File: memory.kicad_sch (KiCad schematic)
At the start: 22 parts, among them U2 IS42S16160J-6BLI, U3 MX30LF1G18AC-XKI, U4 KLM8G1GETF-B041

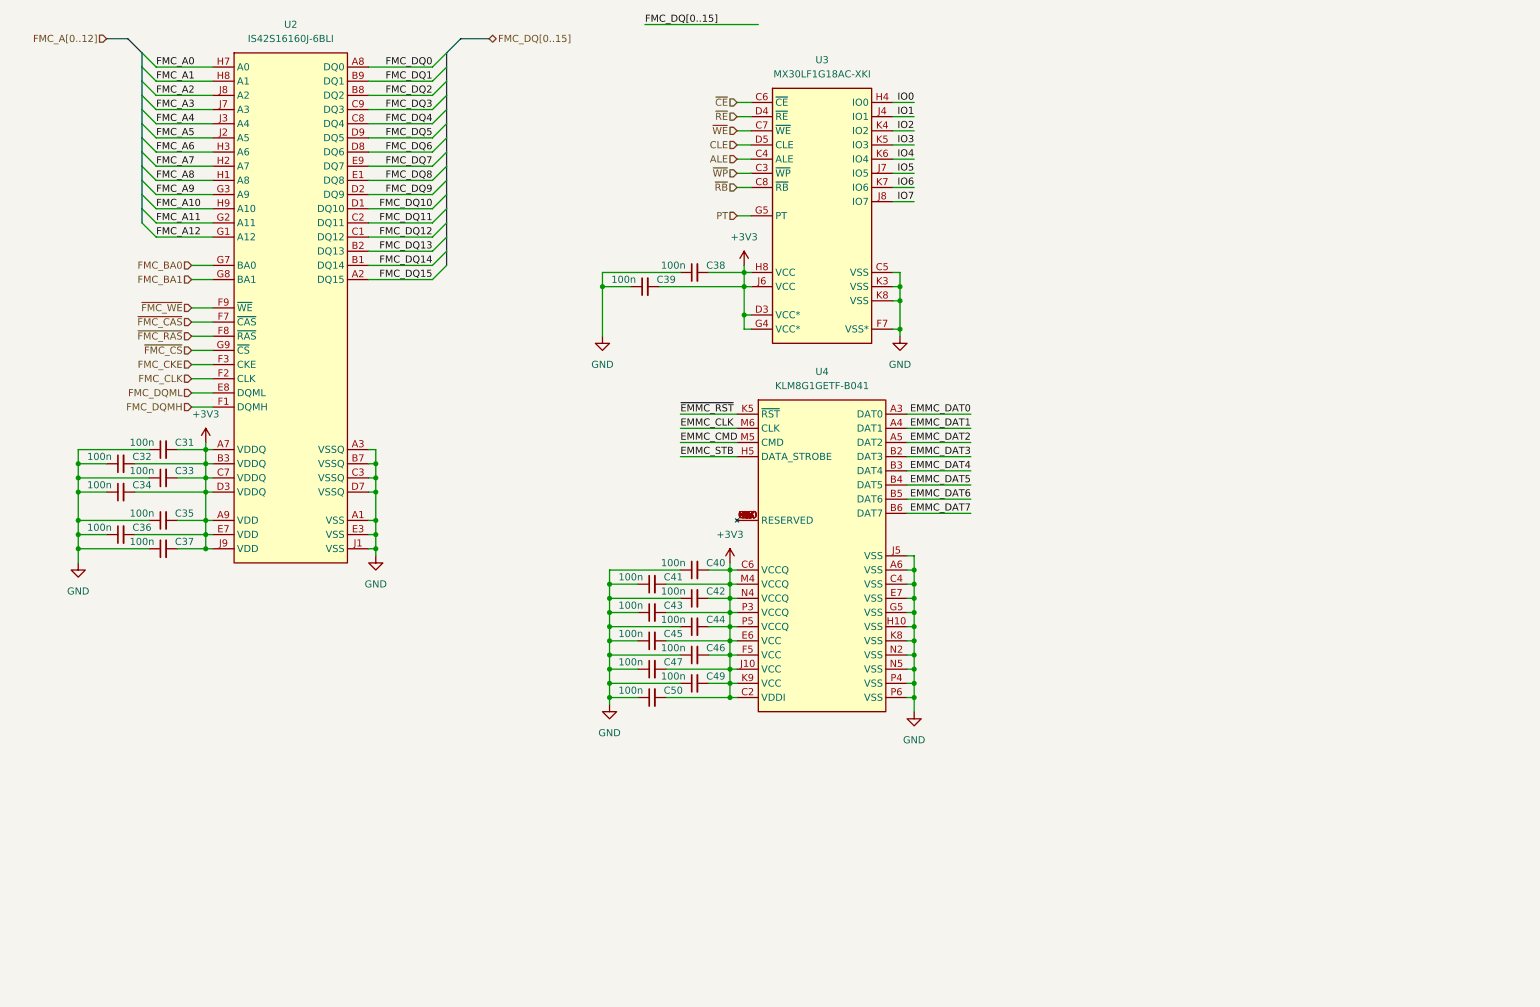
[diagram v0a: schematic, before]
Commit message: Added octospi flash lib
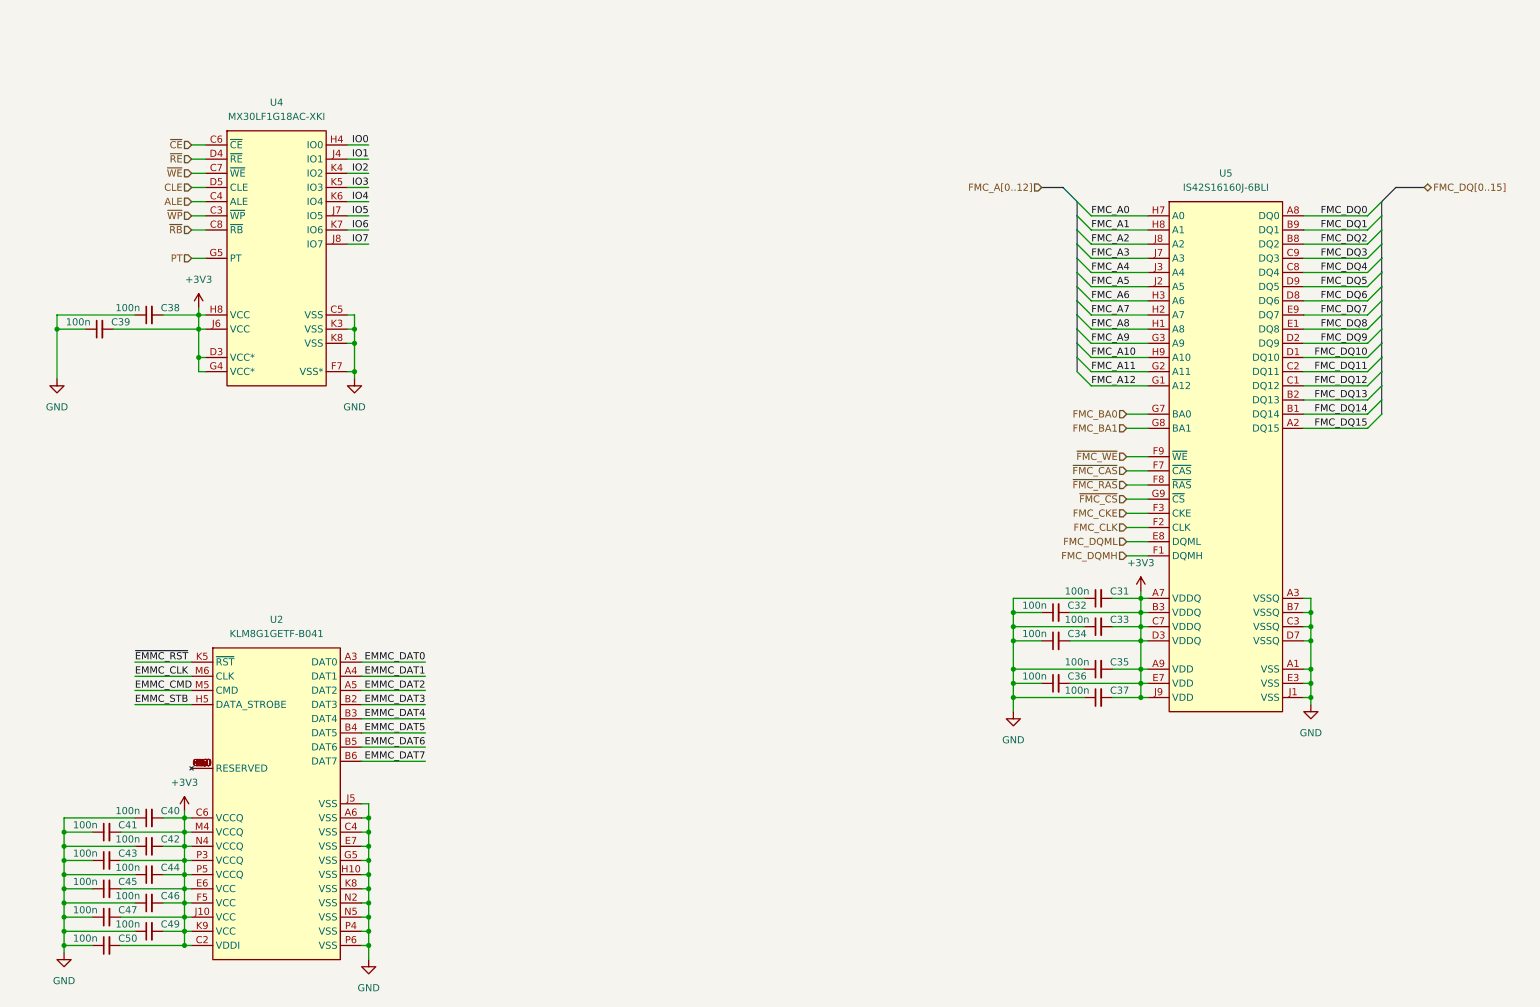
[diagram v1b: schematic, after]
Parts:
- removed U2: IS42S16160J-6BLI, IS42S16160J-6BLI (1):BGA54C80P9X9_800X800X120, symbol Memory_SDRAM:IS42S16160J-BLI-BGA
- removed U3: MX30LF1G18AC-XKI, lib:BGA63C80P10X12_900X1100X100N, symbol Memory_NAND_FLASH:MX30LF1G18AC-XKI
- removed U4: KLM8G1GETF-B041, KLM8G1GETF-B0410:BGA153C50P14X14_1150X1300X80, symbol Memory_EMMC:KLM8G1GETF-B041-Samsung
- added U2: KLM8G1GETF-B041, symbol Memory_EMMC:KLM8G1GETF-B041-Samsung
- added U4: MX30LF1G18AC-XKI, symbol Memory_NAND_FLASH:MX30LF1G18AC-XKI
- added U5: IS42S16160J-6BLI, symbol Memory_SDRAM:IS42S16160J-6BLI-BGA
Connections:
- net +3V3: now also U2.C2 (VDDI), U2.C6 (VCCQ), U2.E6 (VCC), U2.F5 (VCC), U2.J10 (VCC), U2.K9 (VCC), U2.M4 (VCCQ), U2.N4 (VCCQ), U2.P3 (VCCQ), U2.P5 (VCCQ), U4.D3 (VCC*), U4.G4 (VCC*), U4.H8 (VCC), U4.J6 (VCC), U5.A7 (VDDQ), U5.A9 (VDD), U5.B3 (VDDQ), U5.C7 (VDDQ), U5.D3 (VDDQ), U5.E7 (VDD), U5.J9 (VDD)
- net ALE: now also U4.C4 (ALE)
- net CLE: now also U4.D5 (CLE)
- net EMMC_CLK: now also U2.M6 (CLK)
- net EMMC_CMD: now also U2.M5 (CMD)
- net EMMC_DAT0: now also U2.A3 (DAT0)
- net EMMC_DAT1: now also U2.A4 (DAT1)
- net EMMC_DAT2: now also U2.A5 (DAT2)
- net EMMC_DAT3: now also U2.B2 (DAT3)
- net EMMC_DAT4: now also U2.B3 (DAT4)
- net EMMC_DAT5: now also U2.B4 (DAT5)
- net EMMC_DAT6: now also U2.B5 (DAT6)
- net EMMC_DAT7: now also U2.B6 (DAT7)
- net EMMC_STB: now also U2.H5 (DATA_STROBE)
- net FMC_A0: now also U5.H7 (A0)
- net FMC_A1: now also U5.H8 (A1)
- net FMC_A10: now also U5.H9 (A10)
- net FMC_A11: now also U5.G2 (A11)
- net FMC_A12: now also U5.G1 (A12)
- net FMC_A2: now also U5.J8 (A2)
- net FMC_A3: now also U5.J7 (A3)
- net FMC_A4: now also U5.J3 (A4)
- net FMC_A5: now also U5.J2 (A5)
- net FMC_A6: now also U5.H3 (A6)
- net FMC_A7: now also U5.H2 (A7)
- net FMC_A8: now also U5.H1 (A8)
- net FMC_A9: now also U5.G3 (A9)
- net FMC_BA0: now also U5.G7 (BA0)
- net FMC_BA1: now also U5.G8 (BA1)
- net FMC_CKE: now also U5.F3 (CKE)
- net FMC_CLK: now also U5.F2 (CLK)
- net FMC_DQ0: now also U5.A8 (DQ0)
- net FMC_DQ1: now also U5.B9 (DQ1)
- net FMC_DQ10: now also U5.D1 (DQ10)
- net FMC_DQ11: now also U5.C2 (DQ11)
- net FMC_DQ12: now also U5.C1 (DQ12)
- net FMC_DQ13: now also U5.B2 (DQ13)
- net FMC_DQ14: now also U5.B1 (DQ14)
- net FMC_DQ15: now also U5.A2 (DQ15)
- net FMC_DQ2: now also U5.B8 (DQ2)
- net FMC_DQ3: now also U5.C9 (DQ3)
- net FMC_DQ4: now also U5.C8 (DQ4)
- net FMC_DQ5: now also U5.D9 (DQ5)
- net FMC_DQ6: now also U5.D8 (DQ6)
- net FMC_DQ7: now also U5.E9 (DQ7)
- net FMC_DQ8: now also U5.E1 (DQ8)
- net FMC_DQ9: now also U5.D2 (DQ9)
- net FMC_DQMH: now also U5.F1 (DQMH)
- net FMC_DQML: now also U5.E8 (DQML)
- net GND: now also U2.A6 (VSS), U2.C4 (VSS), U2.E7 (VSS), U2.G5 (VSS), U2.H10 (VSS), U2.J5 (VSS), U2.K8 (VSS), U2.N2 (VSS), U2.N5 (VSS), U2.P4 (VSS), U2.P6 (VSS), U4.C5 (VSS), U4.F7 (VSS*), U4.K3 (VSS), U4.K8 (VSS), U5.A1 (VSS), U5.A3 (VSSQ), U5.B7 (VSSQ), U5.C3 (VSSQ), U5.D7 (VSSQ), U5.E3 (VSS), U5.J1 (VSS)
- net IO0: now also U4.H4 (IO0)
- net IO1: now also U4.J4 (IO1)
- net IO2: now also U4.K4 (IO2)
- net IO3: now also U4.K5 (IO3)
- net IO4: now also U4.K6 (IO4)
- net IO5: now also U4.J7 (IO5)
- net IO6: now also U4.K7 (IO6)
- net IO7: now also U4.J8 (IO7)
- net PT: now also U4.G5 (PT)
- net ~{CE}: now also U4.C6 (~{CE})
- net ~{EMMC_RST}: now also U2.K5 (~{RST})
- net ~{FMC_CAS}: now also U5.F7 (~{CAS})
- net ~{FMC_CS}: now also U5.G9 (~{CS})
- net ~{FMC_RAS}: now also U5.F8 (~{RAS})
- net ~{FMC_WE}: now also U5.F9 (~{WE})
- net ~{RB}: now also U4.C8 (~{RB})
- net ~{RE}: now also U4.D4 (~{RE})
- net ~{WE}: now also U4.C7 (~{WE})
- net ~{WP}: now also U4.C3 (~{WP})
- new net: U2.A1 (NC), U2.A10 (NC), U2.A11 (NC), U2.A12 (NC), U2.A13 (NC), U2.A14 (NC), U2.A2 (NC), U2.A8 (NC), U2.A9 (NC), U2.B1 (NC), U2.B10 (NC), U2.B11 (NC), U2.B12 (NC), U2.B13 (NC), U2.B14 (NC), U2.B7 (NC), U2.B8 (NC), U2.B9 (NC), U2.C1 (NC), U2.C10 (NC), U2.C11 (NC), U2.C12 (NC), U2.C13 (NC), U2.C14 (NC), U2.C3 (NC), U2.C5 (NC), U2.C7 (NC), U2.C8 (NC), U2.C9 (NC), U2.D1 (NC), U2.D12 (NC), U2.D13 (NC), U2.D14 (NC), U2.D2 (NC), U2.D3 (NC), U2.D4 (NC), U2.E1 (NC), U2.E12 (NC), U2.E13 (NC), U2.E14 (NC), U2.E2 (NC), U2.E3 (NC), U2.F1 (NC), U2.F12 (NC), U2.F13 (NC), U2.F14 (NC), U2.F2 (NC), U2.F3 (NC), U2.G1 (NC), U2.G12 (NC), U2.G13 (NC), U2.G14 (NC), U2.G2 (NC), U2.H1 (NC), U2.H12 (NC), U2.H13 (NC), U2.H14 (NC), U2.H2 (NC), U2.H3 (NC), U2.J1 (NC), U2.J12 (NC), U2.J13 (NC), U2.J14 (NC), U2.J2 (NC), U2.J3 (NC), U2.K1 (NC), U2.K12 (NC), U2.K13 (NC), U2.K14 (NC), U2.K2 (NC), U2.K3 (NC), U2.L1 (NC), U2.L12 (NC), U2.L13 (NC), U2.L14 (NC), U2.L2 (NC), U2.L3 (NC), U2.M1 (NC), U2.M10 (NC), U2.M11 (NC), U2.M12 (NC), U2.M13 (NC), U2.M14 (NC), U2.M2 (NC), U2.M3 (NC), U2.M7 (NC), U2.M8 (NC), U2.M9 (NC), U2.N1 (NC), U2.N10 (NC), U2.N11 (NC), U2.N12 (NC), U2.N13 (NC), U2.N14 (NC), U2.N3 (NC), U2.N6 (NC), U2.N7 (NC), U2.N8 (NC), U2.N9 (NC), U2.P1 (NC), U2.P11 (NC), U2.P12 (NC), U2.P13 (NC), U2.P14 (NC), U2.P2 (NC), U2.P8 (NC), U2.P9 (NC)
- new net: U2.A7 (RESERVED), U2.E10 (RESERVED), U2.E5 (RESERVED), U2.E8 (RESERVED), U2.E9 (RESERVED), U2.F10 (RESERVED), U2.G10 (RESERVED), U2.G3 (RESERVED), U2.K10 (RESERVED), U2.K6 (RESERVED), U2.K7 (RESERVED), U2.P10 (RESERVED), U2.P7 (RESERVED)
- new net: U4.A1 (NC), U4.A10 (NC), U4.A2 (NC), U4.A9 (NC), U4.B1 (NC), U4.B10 (NC), U4.B9 (NC), U4.D6 (NC), U4.D7 (NC), U4.D8 (NC), U4.E3 (NC), U4.E4 (NC), U4.E5 (NC), U4.E6 (NC), U4.E7 (NC), U4.E8 (NC), U4.F3 (NC), U4.F4 (NC), U4.F5 (NC), U4.F6 (NC), U4.F8 (NC), U4.G3 (NC), U4.G6 (NC), U4.G7 (NC), U4.G8 (NC), U4.H3 (NC), U4.H5 (NC), U4.H6 (NC), U4.H7 (NC), U4.J3 (NC), U4.J5 (NC), U4.L1 (NC), U4.L10 (NC), U4.L2 (NC), U4.L9 (NC), U4.M1 (NC), U4.M10 (NC), U4.M2 (NC), U4.M9 (NC)
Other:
- moved on the sheet: C31, C32, C33, C34, C35, C36, C37, C38, C39, C40, C41, C42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
